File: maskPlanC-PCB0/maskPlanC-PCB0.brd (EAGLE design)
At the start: 23 x 18 mm, 9 parts, among them U1 ATTINY85-20PU

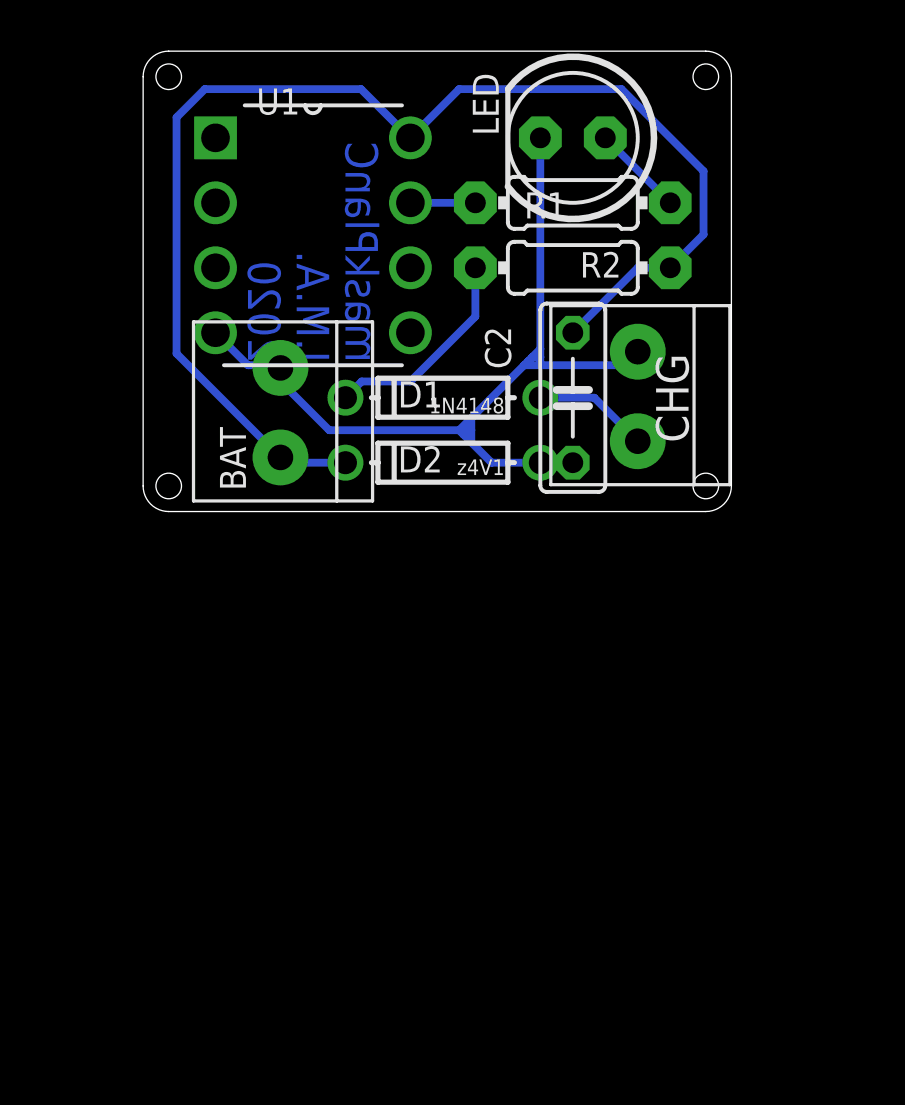
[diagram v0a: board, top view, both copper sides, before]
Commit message: added PCB & software for matrix2
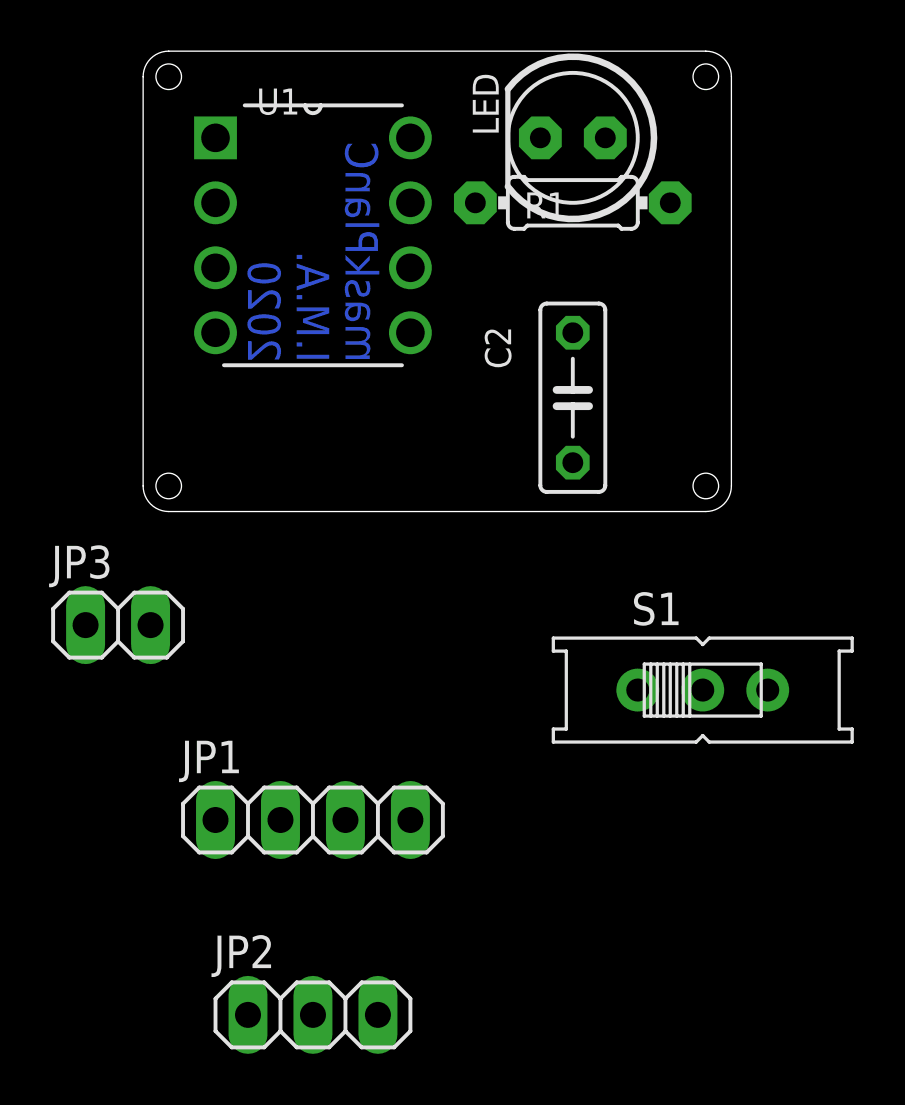
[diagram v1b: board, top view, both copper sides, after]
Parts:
- removed BAT, CHG: 1X2-3.5MM, adafruit:1X2-3.5MM
- removed D1: 1N4148, adafruit:DO-1N4148
- removed D2: z4V1, adafruit:DO-1N4148
- removed R2: 1k, adafruit:0204/7
- added JP1: (no value), pinhead:1X04
- added JP2: (no value), pinhead:1X03
- added JP3: (no value), pinhead:1X02
- added S1: EG1218S, EG1218:EG1218
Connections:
- removed net VCC: CHG.2, D1.A
- new net N$3: JP3.2, S1.P
- new net N$4: JP1.2
- new net N$5: JP2.2, U1.2
- new net N$7: JP1.4, U1.7
- net GND: now also JP1.3, JP2.3, JP3.1; no longer BAT.1, CHG.1, D2.A
- net N$1: now also JP1.1, U1.6; no longer R1.1, U1.7
- net N$6: now also R1.1, U1.5; no longer D1.C, R2.1
- net V_BATT: now also JP2.1, S1.O; no longer BAT.2, D2.C, R2.2
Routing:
- net V_BATT: track 50.9 -> 0.00 mm
- net GND: track 36.1 -> 0.00 mm
- net N$6: track 8.30 -> 0.00 mm
- net VCC: track 4.51 -> 0.00 mm
- net N$2: track 3.59 -> 0.00 mm
- net N$1: track 2.54 -> 0.00 mm
